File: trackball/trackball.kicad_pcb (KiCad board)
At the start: 2 copper layers, 15 x 27.4 mm, 7 parts, among them P8 CONN_7, U1 TLE4964-5M, U2 TLE4964-5M, U3 TLE4964-5M, U4 TLE4964-5M

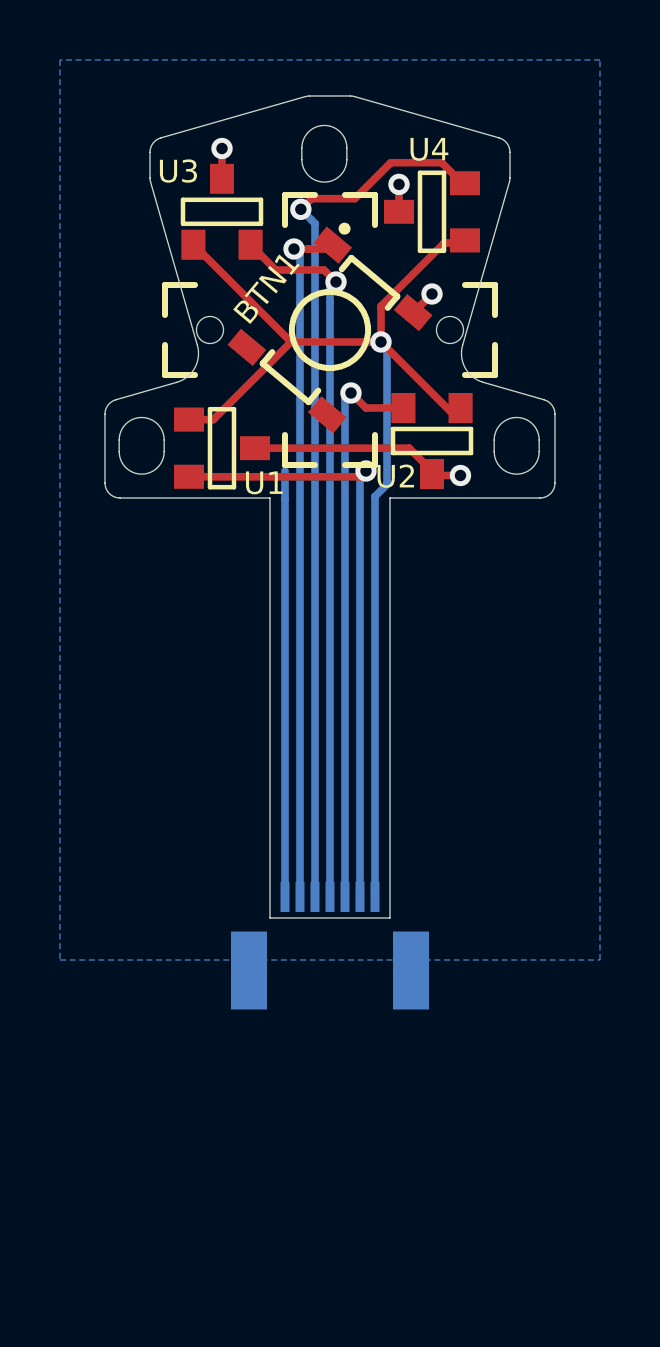
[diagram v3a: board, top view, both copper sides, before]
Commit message: Change FFC connector footprint to FPC pads.
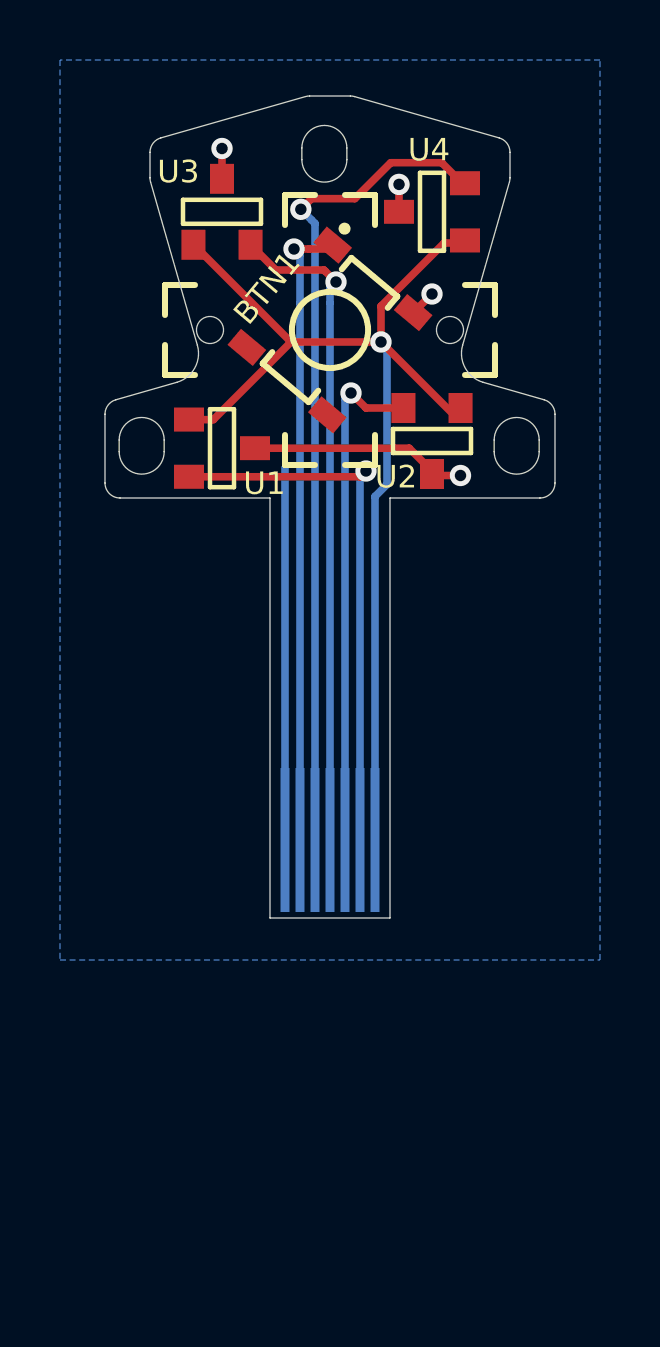
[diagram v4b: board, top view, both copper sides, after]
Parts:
- P8: footprint UGL:FFC_Connector_51281-0794 -> UGL:FPC_Pads_7pin_0.5mm
- moved P8 3.30 mm to (200.0, 169.6)
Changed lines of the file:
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@@
     (thickness 1.6)
     (drawings 46)
-    (tracks 67)
+    (tracks 66)
     (zones 0)
     (modules 7)
@@
     (add_net GND)
   )
-  (module UGL:FFC_Connector_51281-0794 (layer B.Cu)
-    (at 200 172.9 180)
-    (attr smd)
-    (fp_text reference P8 (at -2.5 4.2 180) (layer B.SilkS)
-      (effects (font (size 0.75 0.75) (thickness 0.15)) (justify mirror))
-    )
-    (fp_text value CONN_7 (at 0.1 5.6 180) (layer B.SilkS) hide
-      (effects (font (size 0.75 0.75) (thickness 0.15)) (justify mirror))
-    )
-    (fp_line (start -2.8 3.55) (end -2.8 3) (layer B.SilkS) (width 0.15))
-    (fp_line (start 2.05 3.55) (end 2.8 3.55) (layer B.SilkS) (width 0.15))
-    (fp_line (start 2.8 3.55) (end 2.8 3) (layer B.SilkS) (width 0.15))
-    (fp_line (start -2.8 0) (end 2.8 0) (layer Margin) (width 0.15))
-    (fp_line (start -2.8 3.55) (end -2.05 3.55) (layer B.SilkS) (width 0.15))
-    (pad 2 smd rect (at -1 4 180) (size 0.3 1) (layers B.Cu B.Paste B.Mask)
-      (net 3 /TB_LEFT) (clearance 0.1778))
-    (pad 5 smd rect (at 0.5 4 180) (size 0.3 1) (layers B.Cu B.Paste B.Mask)
-      (net 7 /TB_RIGHT) (clearance 0.1778))
-    (pad "" smd rect (at 2.7 1.55 180) (size 1.2 2.6) (layers B.Cu B.Paste B.Mask))
-    (pad 3 smd rect (at -0.5 4 180) (size 0.3 1) (layers B.Cu B.Paste B.Mask)
-      (net 5 /TB_DOWN) (clearance 0.1778))
-    (pad 4 smd rect (at 0 4 180) (size 0.3 1) (layers B.Cu B.Paste B.Mask)
-      (net 6 /TB_UP) (clearance 0.1778))
-    (pad "" smd rect (at -2.7 1.55 180) (size 1.2 2.6) (layers B.Cu B.Paste B.Mask))
-    (pad 1 smd rect (at -1.5 4 180) (size 0.3 1) (layers B.Cu B.Paste B.Mask)
-      (net 4 +3V3) (clearance 0.1778))
-    (pad 6 smd rect (at 1 4 180) (size 0.3 1) (layers B.Cu B.Paste B.Mask)
-      (net 2 /TB_BTN) (clearance 0.1778))
-    (pad 7 smd rect (at 1.5 4 180) (size 0.3 1) (layers B.Cu B.Paste B.Mask)
-      (net 1 GND) (clearance 0.1778))
-  )
   (module UGL:SOT-23 (layer F.Cu)
     (at 196.4 146.06)
@@
       (net 2 /TB_BTN))
     (pad 4 smd rect (at -2.225 -1.75 230) (size 0.7 1.1) (layers F.Cu F.Paste F.Mask))
+  )
+  (module UGL:FPC_Pads_7pin_0.5mm (layer B.Cu)
+    (at 200 169.6 180)
+    (attr virtual)
+    (fp_text reference P8 (at 0 5.9) (layer B.SilkS) hide
+      (effects (font (size 0.75 0.75) (thickness 0.15)) (justify mirror))
+    )
+    (fp_text value CONN_7 (at 0 -0.75) (layer B.SilkS) hide
+      (effects (font (size 0.75 0.75) (thickness 0.15)) (justify mirror))
+    )
+    (pad 7 smd rect (at 1.5 2.6 180) (size 0.3 4.8) (layers B.Cu B.Paste B.Mask)
+      (net 1 GND) (clearance 0.1778))
+    (pad 6 smd rect (at 1 2.6 180) (size 0.3 4.8) (layers B.Cu B.Paste B.Mask)
+      (net 2 /TB_BTN) (clearance 0.1778))
+    (pad 1 smd rect (at -1.5 2.6 180) (size 0.3 4.8) (layers B.Cu B.Paste B.Mask)
+      (net 4 +3V3) (clearance 0.1778))
+    (pad 4 smd rect (at 0 2.6 180) (size 0.3 4.8) (layers B.Cu B.Paste B.Mask)
+      (net 6 /TB_UP) (clearance 0.1778))
+    (pad 3 smd rect (at -0.5 2.6 180) (size 0.3 4.8) (layers B.Cu B.Paste B.Mask)
+      (net 5 /TB_DOWN) (clearance 0.1778))
+    (pad 5 smd rect (at 0.5 2.6 180) (size 0.3 4.8) (layers B.Cu B.Paste B.Mask)
+      (net 7 /TB_RIGHT) (clearance 0.1778))
+    (pad 2 smd rect (at -1 2.6 180) (size 0.3 4.8) (layers B.Cu B.Paste B.Mask)
+      (net 3 /TB_LEFT) (clearance 0.1778))
   )
   (gr_line (start 202 155.6) (end 207 155.6) (angle 90) (layer Edge.Cuts) (width 0.01))
@@
   (gr_line (start 202 169.6) (end 198 169.6) (angle 90) (layer Edge.Cuts) (width 0.01))
   (gr_line (start 198 164.6) (end 202 164.6) (angle 90) (layer Margin) (width 0.01))
+  (segment (start 198.5 154.6) (end 198.5 169.26479) (width 0.254) (layer B.Cu) (net 1))
   (via (at 196.4 143.95) (size 0.7112) (drill 0.381) (layers F.Cu B.Cu) (net 1))
   (segment (start 203.4 155.03982) (end 203.58982 154.85) (width 0.254) (layer F.Cu) (net 1))
@@
   (segment (start 202.77078 149.420429) (end 202.779571 149.420429) (width 0.254) (layer F.Cu) (net 1))
   (segment (start 202.779571 149.420429) (end 203.4 148.8) (width 0.254) (layer F.Cu) (net 1))
-  (segment (start 198.5 168.9) (end 198.5 155.625942) (width 0.254) (layer B.Cu) (net 1))
-  (segment (start 198.5 155.625942) (end 198.5 154.7) (width 0.254) (layer B.Cu) (net 1))
   (segment (start 199 149.1) (end 199 169.26479) (width 0.254) (layer B.Cu) (net 2))
   (via (at 198.8 147.3) (size 0.7112) (drill 0.381) (layers F.Cu B.Cu) (net 2))

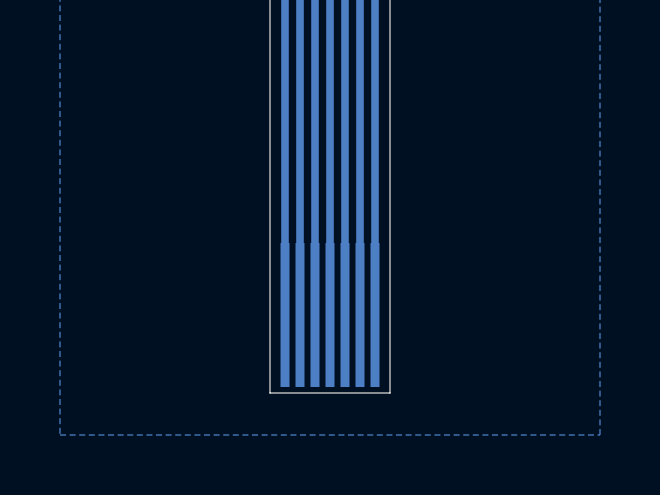
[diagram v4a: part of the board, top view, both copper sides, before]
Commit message: Update FPC pads.
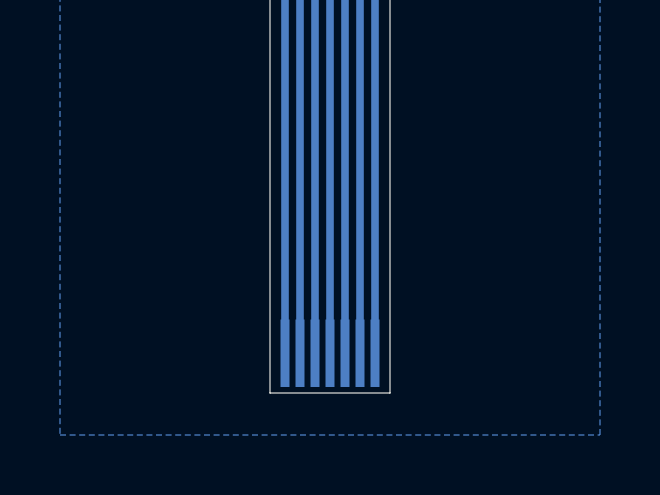
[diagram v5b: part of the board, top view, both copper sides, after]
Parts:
- moved P8 0.20 mm to (200.0, 169.4)
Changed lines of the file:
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@@
     (add_net GND)
+  )
+  (module UGL:FPC_Pads_7pin_0.5mm (layer B.Cu)
+    (at 200 169.4 180)
+    (attr virtual)
+    (fp_text reference P8 (at 0 5.9) (layer B.SilkS) hide
+      (effects (font (size 0.75 0.75) (thickness 0.15)) (justify mirror))
+    )
+    (fp_text value CONN_7 (at 0 -0.75) (layer B.SilkS) hide
+      (effects (font (size 0.75 0.75) (thickness 0.15)) (justify mirror))
+    )
+    (pad 7 smd rect (at 1.5 1.125 180) (size 0.3 2.25) (layers B.Cu B.Paste B.Mask)
+      (net 1 GND) (clearance 0.1778))
+    (pad 6 smd rect (at 1 1.125 180) (size 0.3 2.25) (layers B.Cu B.Paste B.Mask)
+      (net 2 /TB_BTN) (clearance 0.1778))
+    (pad 1 smd rect (at -1.5 1.125 180) (size 0.3 2.25) (layers B.Cu B.Paste B.Mask)
+      (net 4 +3V3) (clearance 0.1778))
+    (pad 4 smd rect (at 0 1.125 180) (size 0.3 2.25) (layers B.Cu B.Paste B.Mask)
+      (net 6 /TB_UP) (clearance 0.1778))
+    (pad 3 smd rect (at -0.5 1.125 180) (size 0.3 2.25) (layers B.Cu B.Paste B.Mask)
+      (net 5 /TB_DOWN) (clearance 0.1778))
+    (pad 5 smd rect (at 0.5 1.125 180) (size 0.3 2.25) (layers B.Cu B.Paste B.Mask)
+      (net 7 /TB_RIGHT) (clearance 0.1778))
+    (pad 2 smd rect (at -1 1.125 180) (size 0.3 2.25) (layers B.Cu B.Paste B.Mask)
+      (net 3 /TB_LEFT) (clearance 0.1778))
   )
   (module UGL:SOT-23 (layer F.Cu)
@@
     (pad 4 smd rect (at -2.225 -1.75 230) (size 0.7 1.1) (layers F.Cu F.Paste F.Mask))
   )
-  (module UGL:FPC_Pads_7pin_0.5mm (layer B.Cu)
-    (at 200 169.6 180)
-    (attr virtual)
-    (fp_text reference P8 (at 0 5.9) (layer B.SilkS) hide
-      (effects (font (size 0.75 0.75) (thickness 0.15)) (justify mirror))
-    )
-    (fp_text value CONN_7 (at 0 -0.75) (layer B.SilkS) hide
-      (effects (font (size 0.75 0.75) (thickness 0.15)) (justify mirror))
-    )
-    (pad 7 smd rect (at 1.5 2.6 180) (size 0.3 4.8) (layers B.Cu B.Paste B.Mask)
-      (net 1 GND) (clearance 0.1778))
-    (pad 6 smd rect (at 1 2.6 180) (size 0.3 4.8) (layers B.Cu B.Paste B.Mask)
-      (net 2 /TB_BTN) (clearance 0.1778))
-    (pad 1 smd rect (at -1.5 2.6 180) (size 0.3 4.8) (layers B.Cu B.Paste B.Mask)
-      (net 4 +3V3) (clearance 0.1778))
-    (pad 4 smd rect (at 0 2.6 180) (size 0.3 4.8) (layers B.Cu B.Paste B.Mask)
-      (net 6 /TB_UP) (clearance 0.1778))
-    (pad 3 smd rect (at -0.5 2.6 180) (size 0.3 4.8) (layers B.Cu B.Paste B.Mask)
-      (net 5 /TB_DOWN) (clearance 0.1778))
-    (pad 5 smd rect (at 0.5 2.6 180) (size 0.3 4.8) (layers B.Cu B.Paste B.Mask)
-      (net 7 /TB_RIGHT) (clearance 0.1778))
-    (pad 2 smd rect (at -1 2.6 180) (size 0.3 4.8) (layers B.Cu B.Paste B.Mask)
-      (net 3 /TB_LEFT) (clearance 0.1778))
-  )
   (gr_line (start 202 155.6) (end 207 155.6) (angle 90) (layer Edge.Cuts) (width 0.01))
